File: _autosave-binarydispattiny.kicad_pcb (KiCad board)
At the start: 2 copper layers, 61.8 x 40.5 mm, 32 parts, among them J1 Conn_01x02_Male, J2 Conn_01x08, J3 AVR-TPI-6, Q1 DMMT5401, U1 4021, U2 ATtiny102-SS, U3 19x12mm 7segment, U4 MAX7219, U5 19x12mm 7segment

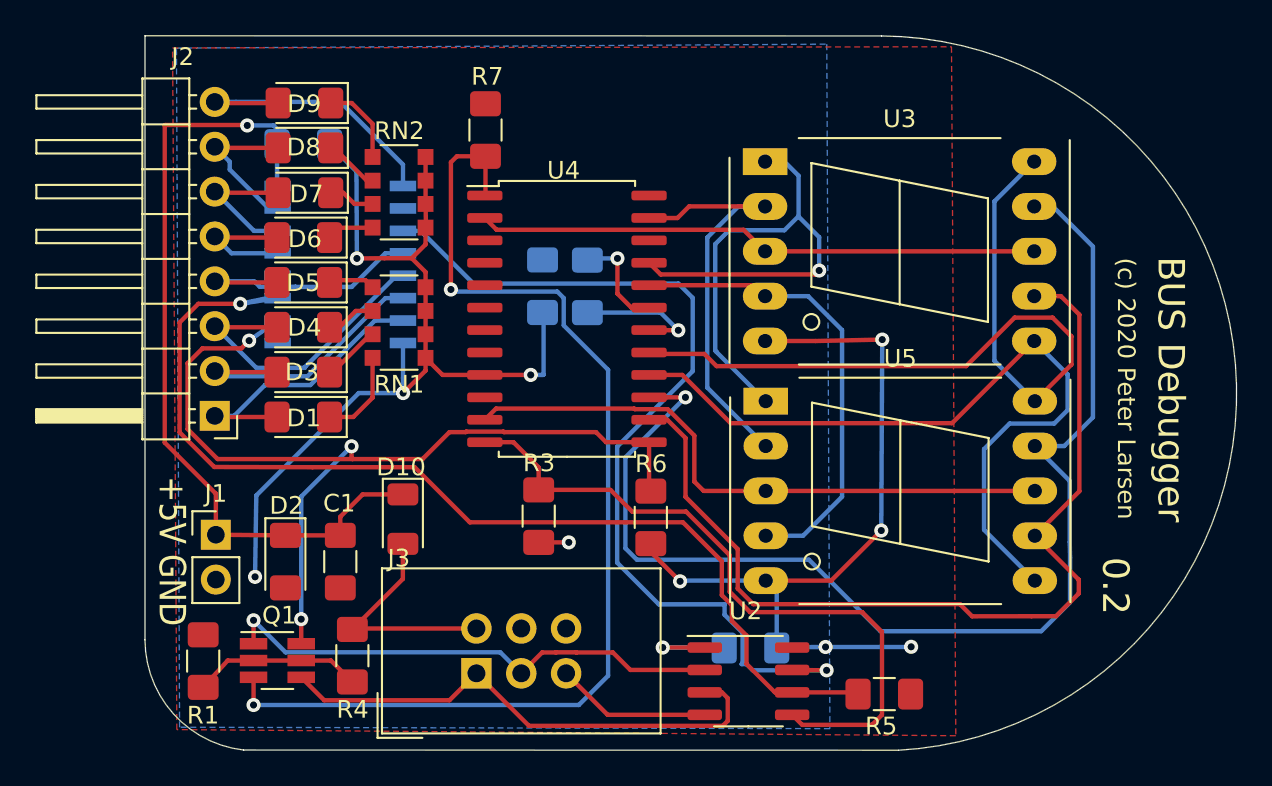
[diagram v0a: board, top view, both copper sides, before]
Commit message: Fixed MAX7912 sizing
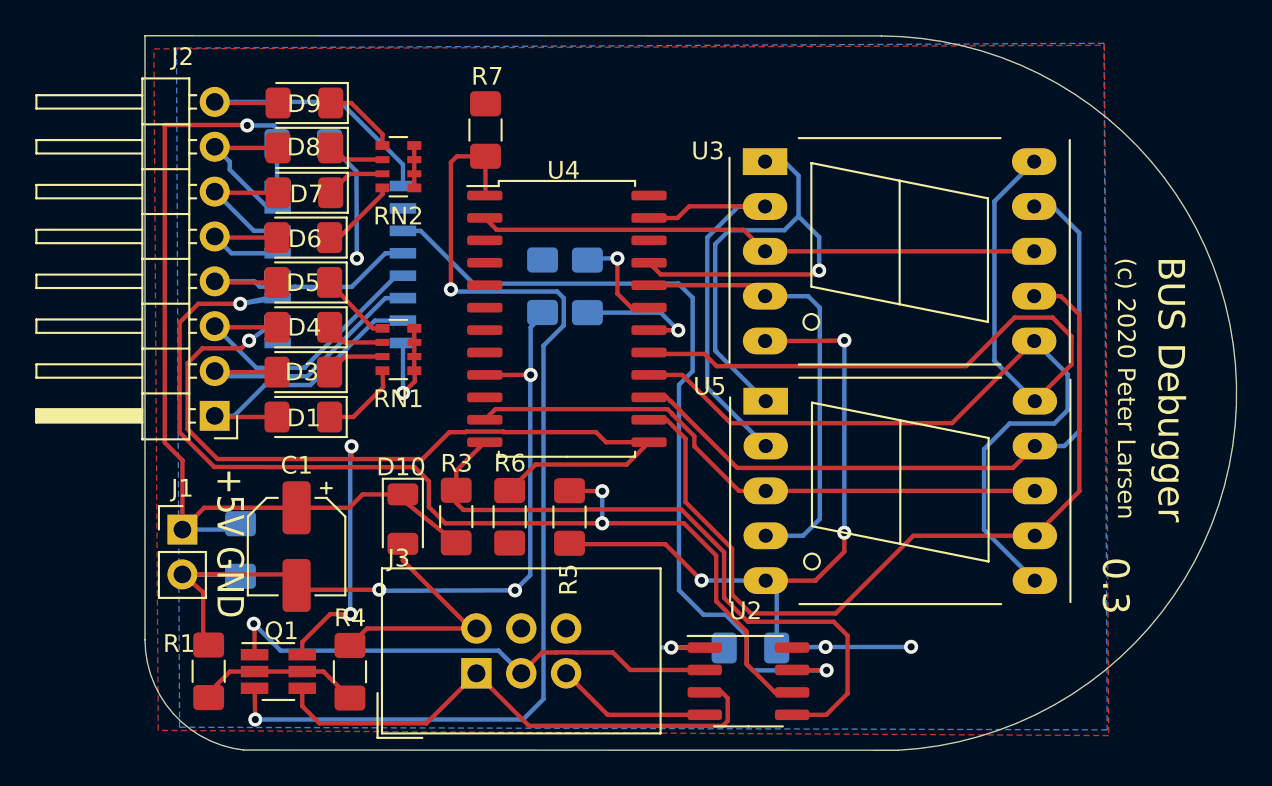
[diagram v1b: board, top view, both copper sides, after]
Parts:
- C1: footprint Capacitor_SMD:C_1206_3216Metric_Pad1.42x1.75mm_HandSolder -> Capacitor_SMD:CP_Elec_5x5.4
- D2: moved to B.Cu
- RN1, RN2: footprint Resistor_SMD:R_Array_Convex_4x1206 -> Resistor_SMD:R_Array_Convex_4x0603
- moved R5 20.5 mm to (134.3, 101.5), turned to 270 degrees
- moved R6 8.00 mm to (130.9, 101.5)
- moved R3 4.67 mm to (127.9, 101.5)
- moved D2 2.62 mm to (115.7, 103.4)
- moved C1 2.62 mm to (118.9, 103.2)
- moved J1 1.91 mm to (112.4, 102.3)
- moved RN1 1.52 mm to (124.6, 92.1)
- moved RN2 1.45 mm to (124.6, 81.7)
- moved R4 0.92 mm to (121.9, 110.3)
- moved R1 0.66 mm to (113.9, 110.3)
- moved Q1 0.63 mm to (117.8, 110.3)
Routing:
- net /SEG_F: track 67.4 -> 41.3 mm, vias 1 -> 0
- net GND: track 98.4 -> 107.3 mm, vias 9 -> 10
- net SHARED_CLK: track 53.5 -> 61.0 mm
- net /SEG_A: track 53.6 -> 48.4 mm
- net +5V: track 59.9 -> 65.0 mm, vias 4 -> 3
- net INDATA: track 52.5 -> 48.0 mm
- net OUTDATA: track 63.7 -> 60.7 mm
- net Net-(D6-Pad1): track 3.44 -> 5.15 mm
- net Net-(D5-Pad1): track 2.65 -> 4.12 mm
- net TPIDATA: track 29.4 -> 30.8 mm
- net SEL_OUT: track 39.2 -> 37.8 mm
- net /DIG_1: track 34.9 -> 33.7 mm
- net /AVR-5v: track 13.2 -> 14.4 mm
- net /SEG_C: track 26.7 -> 25.6 mm
- net SEL_IN: track 60.8 -> 61.6 mm, vias 1 -> 3
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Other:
- board text added: "0.3"
- board text removed: "0.2"
